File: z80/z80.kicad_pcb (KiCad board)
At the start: 2 copper layers, 19 parts, among them J1 Conn_02x16_Counter_Clockwise, J2 Conn_02x16_Counter_Clockwise, SW1 SW_DIP_x08, U1 74HC595, U12 74LS174, U13 74LS174, U18 74LS174, U2 74HC595, U21 SST39SF040, U22 74LS174, U23 74LS174, X8.000Mhz1 TFT680

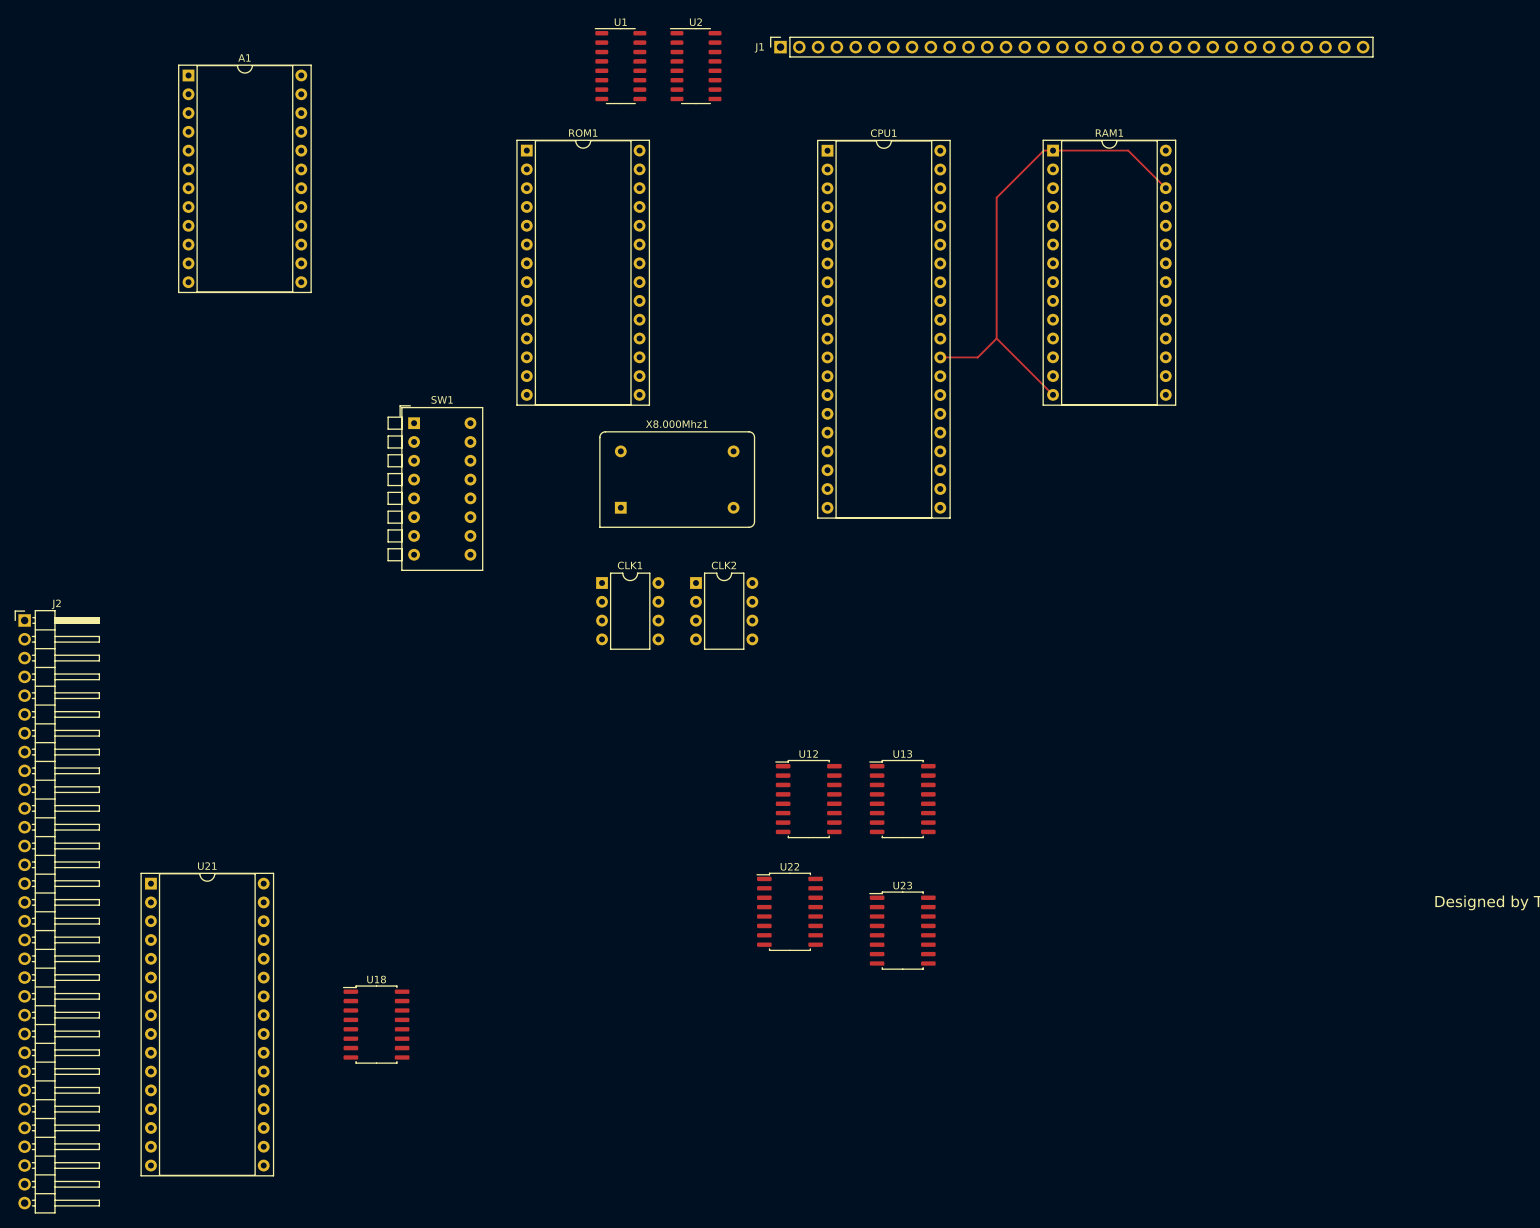
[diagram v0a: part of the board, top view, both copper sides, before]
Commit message: Schematic & eeprom programmer changes
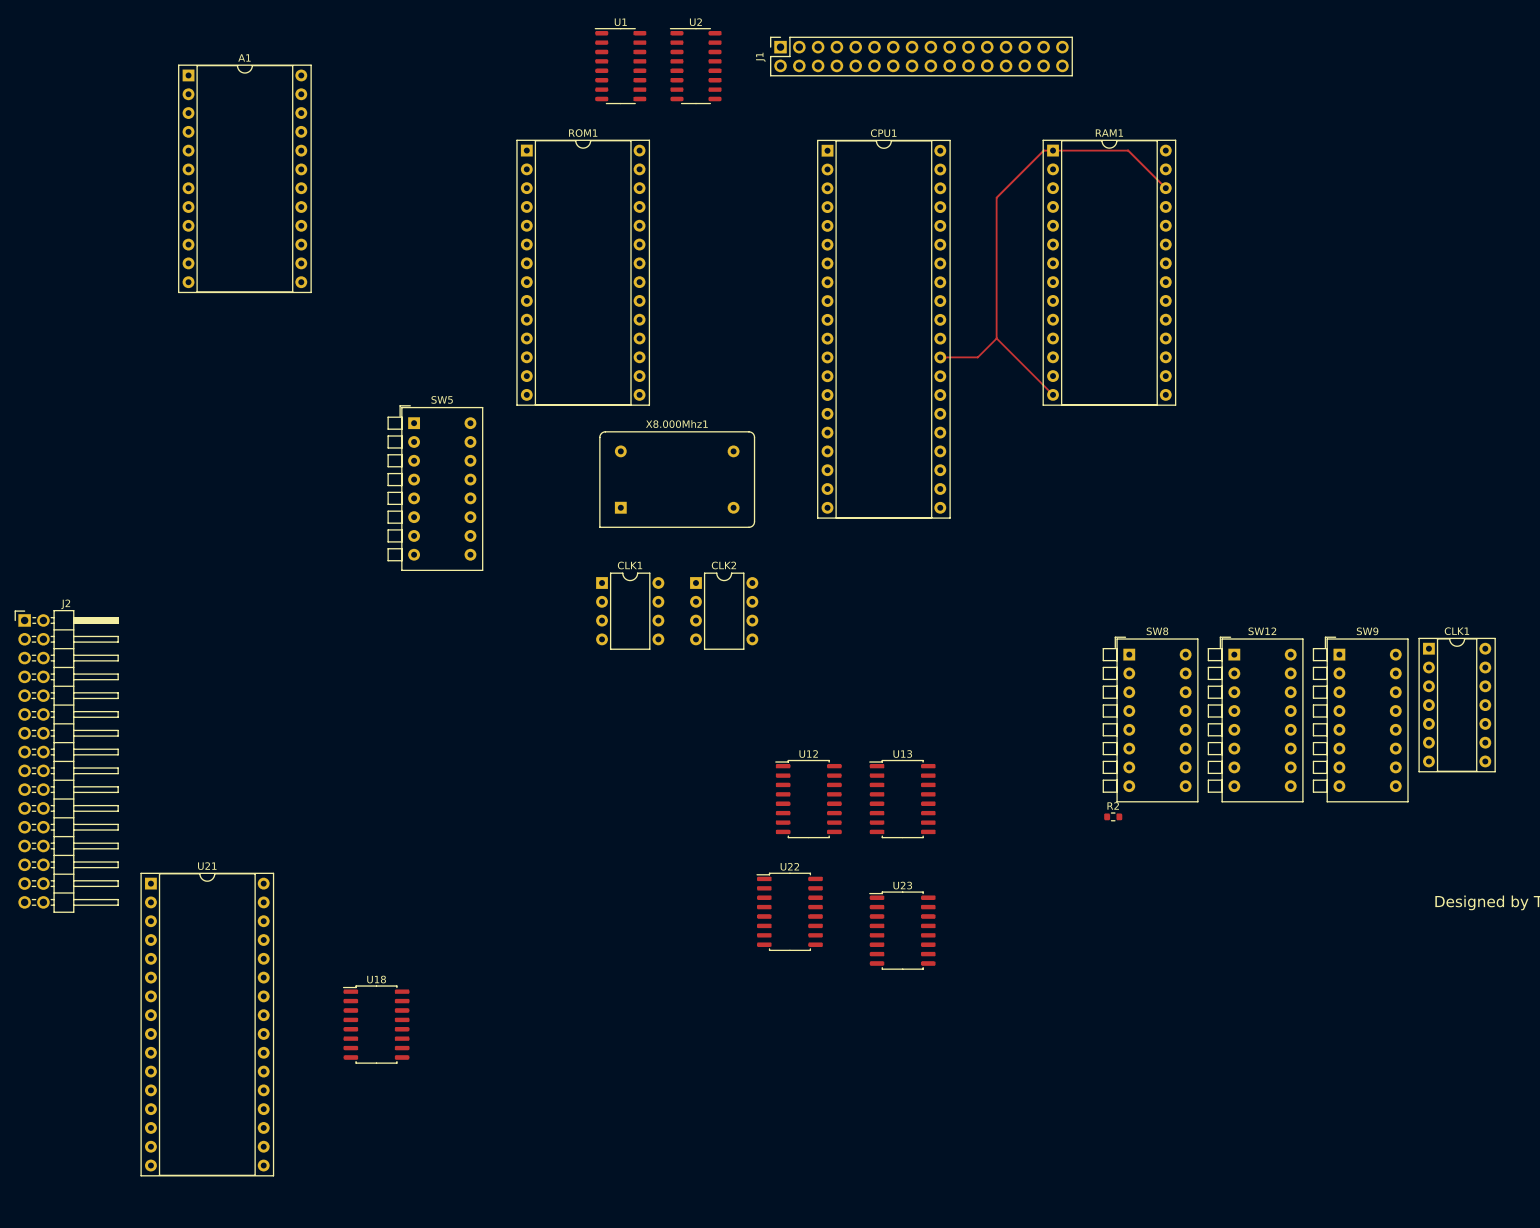
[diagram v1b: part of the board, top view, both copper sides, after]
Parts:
- added CLK1: NE556, Package_DIP:DIP-14_W7.62mm_Socket, F.Cu at (213.4, 119.4)
- added R2: 1K, Resistor_SMD:R_0603_1608Metric, F.Cu at (170.7, 142.1)
- added SW12: SW_DIP_x08, Button_Switch_THT:SW_DIP_SPSTx08_Piano_10.8x21.88mm_W7.62mm_P2.54mm, F.Cu at (187.1, 120.2)
- added SW8: SW_DIP_x08, Button_Switch_THT:SW_DIP_SPSTx08_Piano_10.8x21.88mm_W7.62mm_P2.54mm, F.Cu at (172.9, 120.2)
- added SW9: SW_DIP_x08, Button_Switch_THT:SW_DIP_SPSTx08_Piano_10.8x21.88mm_W7.62mm_P2.54mm, F.Cu at (201.3, 120.2)
- J1: footprint Connector_PinSocket_2.54mm:PinSocket_1x32_P2.54mm_Vertical -> Connector_PinSocket_2.54mm:PinSocket_2x16_P2.54mm_Vertical
- J2: footprint Connector_PinHeader_2.54mm:PinHeader_1x32_P2.54mm_Horizontal -> Connector_PinHeader_2.54mm:PinHeader_2x16_P2.54mm_Horizontal
- renumbered SW1 to SW5
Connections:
- net FstClk renamed /FstClk
- J1 pad 1: unconnected-(J1-Pad1) -> D7
- J1 pad 10: unconnected-(J1-Pad10) -> +5V
- J1 pad 16: unconnected-(J1-Pad16) -> GND
- J1 pad 17: unconnected-(J1-Pad17) -> GND
- J1 pad 18: unconnected-(J1-Pad18) -> A0
- J1 pad 19: unconnected-(J1-Pad19) -> A1
- J1 pad 2: unconnected-(J1-Pad2) -> D6
- J1 pad 20: unconnected-(J1-Pad20) -> A2
- J1 pad 21: unconnected-(J1-Pad21) -> A3
- J1 pad 22: unconnected-(J1-Pad22) -> A4
- J1 pad 23: unconnected-(J1-Pad23) -> A5
- J1 pad 24: unconnected-(J1-Pad24) -> A6
- J1 pad 25: unconnected-(J1-Pad25) -> A7
- J1 pad 26: unconnected-(J1-Pad26) -> A8
- J1 pad 27: unconnected-(J1-Pad27) -> A9
- J1 pad 28: unconnected-(J1-Pad28) -> A10
- J1 pad 29: unconnected-(J1-Pad29) -> A11
- J1 pad 3: unconnected-(J1-Pad3) -> D5
- J1 pad 30: unconnected-(J1-Pad30) -> A12
- J1 pad 31: unconnected-(J1-Pad31) -> A13
- J1 pad 32: unconnected-(J1-Pad32) -> A14
- J1 pad 4: unconnected-(J1-Pad4) -> D4
- J1 pad 5: unconnected-(J1-Pad5) -> D3
- J1 pad 6: unconnected-(J1-Pad6) -> D2
- J1 pad 7: unconnected-(J1-Pad7) -> D1
- J1 pad 8: unconnected-(J1-Pad8) -> D0
- J1 pad 9: unconnected-(J1-Pad9) -> A15
- X8.000Mhz1 pad 1: unconnected-(X8.000Mhz1-Pad1) -> GND

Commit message: schematic and pcb changes
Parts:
- removed the CLK1 at (101.6, 110.5)
- removed CLK2: NE555P, Package_DIP:DIP-8_W7.62mm
- added C1: 1uF, Capacitor_SMD:C_0805_2012Metric_Pad1.18x1.45mm_HandSolder, F.Cu at (133.3, 114.3)
- added C2: 0.1uF, Capacitor_SMD:C_0805_2012Metric_Pad1.18x1.45mm_HandSolder, F.Cu at (171.4, 120.7)
- added C3: 0.1uF, Capacitor_SMD:C_0805_2012Metric_Pad1.18x1.45mm_HandSolder, F.Cu at (144.8, 107.3)
- added C4: 0.1uF, Capacitor_SMD:C_0805_2012Metric_Pad1.18x1.45mm_HandSolder, F.Cu at (133.3, 119.4)
- added C5: 0.1uF, Capacitor_SMD:C_0805_2012Metric_Pad1.18x1.45mm_HandSolder, F.Cu at (133.3, 116.8)
- added C6: 0.1uF, Capacitor_SMD:C_0805_2012Metric_Pad1.18x1.45mm_HandSolder, F.Cu at (151.8, 125.7)
- added C7: 0.1uF, Capacitor_SMD:C_0805_2012Metric_Pad1.18x1.45mm_HandSolder, F.Cu at (151.1, 107.3)
- added D1: LED, LED_SMD:LED_0603_1608Metric_Pad1.05x0.95mm_HandSolder, F.Cu at (129.5, 121.9)
- added D10: LED_Small, LED_SMD:LED_0603_1608Metric_Pad1.05x0.95mm_HandSolder, F.Cu at (151.1, 58.4)
- added D11: LED_Small, LED_SMD:LED_0603_1608Metric_Pad1.05x0.95mm_HandSolder, F.Cu at (168.9, 46.4)
- added D12: LED_Small, LED_SMD:LED_0603_1608Metric_Pad1.05x0.95mm_HandSolder, F.Cu at (168.9, 43.8)
- added D13: LED_Small, LED_SMD:LED_0603_1608Metric_Pad1.05x0.95mm_HandSolder, F.Cu at (168.9, 41.3)
- added D14: LED_Small, LED_SMD:LED_0603_1608Metric_Pad1.05x0.95mm_HandSolder, F.Cu at (168.9, 38.7)
- added D15: LED_Small, LED_SMD:LED_0603_1608Metric_Pad1.05x0.95mm_HandSolder, F.Cu at (168.9, 36.2)
- added D16: LED_Small, LED_SMD:LED_0603_1608Metric_Pad1.05x0.95mm_HandSolder, F.Cu at (168.9, 33.7)
- added D17: LED_Small, LED_SMD:LED_0603_1608Metric_Pad1.05x0.95mm_HandSolder, F.Cu at (168.9, 31.1)
- added D18: LED_Small, LED_SMD:LED_0603_1608Metric_Pad1.05x0.95mm_HandSolder, F.Cu at (168.9, 28.6)
- added D19: LED_Small, LED_SMD:LED_0603_1608Metric_Pad1.05x0.95mm_HandSolder, F.Cu at (165.7, 88.9)
- added D2: LED, LED_SMD:LED_0603_1608Metric_Pad1.05x0.95mm_HandSolder, F.Cu at (129.5, 124.5)
- added D20: LED_Small, LED_SMD:LED_0603_1608Metric_Pad1.05x0.95mm_HandSolder, F.Cu at (165.7, 91.4)
- added D21: LED_Small, LED_SMD:LED_0603_1608Metric_Pad1.05x0.95mm_HandSolder, F.Cu at (165.7, 94.0)
- added D22: LED_Small, LED_SMD:LED_0603_1608Metric_Pad1.05x0.95mm_HandSolder, F.Cu at (165.7, 96.5)
- added D23: LED_Small, LED_SMD:LED_0603_1608Metric_Pad1.05x0.95mm_HandSolder, F.Cu at (165.7, 99.1)
- added D24: LED_Small, LED_SMD:LED_0603_1608Metric_Pad1.05x0.95mm_HandSolder, F.Cu at (165.7, 101.6)
- added D25: LED_Small, LED_SMD:LED_0603_1608Metric_Pad1.05x0.95mm_HandSolder, F.Cu at (165.7, 104.1)
- added D26: LED_Small, LED_SMD:LED_0603_1608Metric_Pad1.05x0.95mm_HandSolder, F.Cu at (165.7, 106.7)
- added D3: LED_Small, LED_SMD:LED_0603_1608Metric_Pad1.05x0.95mm_HandSolder, F.Cu at (151.1, 76.2)
- added D4: LED_Small, LED_SMD:LED_0603_1608Metric_Pad1.05x0.95mm_HandSolder, F.Cu at (151.1, 73.7)
- added D5: LED_Small, LED_SMD:LED_0603_1608Metric_Pad1.05x0.95mm_HandSolder, F.Cu at (151.1, 71.1)
- added D6: LED_Small, LED_SMD:LED_0603_1608Metric_Pad1.05x0.95mm_HandSolder, F.Cu at (151.1, 68.6)
- added D7: LED_Small, LED_SMD:LED_0603_1608Metric_Pad1.05x0.95mm_HandSolder, F.Cu at (151.1, 66.0)
- added D8: LED_Small, LED_SMD:LED_0603_1608Metric_Pad1.05x0.95mm_HandSolder, F.Cu at (151.1, 63.5)
- added D9: LED_Small, LED_SMD:LED_0603_1608Metric_Pad1.05x0.95mm_HandSolder, F.Cu at (151.1, 61.0)
- added R1: 1K, Resistor_SMD:R_0603_1608Metric_Pad0.98x0.95mm_HandSolder, F.Cu at (148.6, 125.7)
- added R10: 10K, Resistor_SMD:R_0603_1608Metric_Pad0.98x0.95mm_HandSolder, F.Cu at (133.3, 124.5)
- added R11: 1K, Resistor_SMD:R_0603_1608Metric_Pad0.98x0.95mm_HandSolder, F.Cu at (256.8, 114.0)
- added R12: 1K, Resistor_SMD:R_0603_1608Metric_Pad0.98x0.95mm_HandSolder, F.Cu at (154.9, 76.2)
- added R13: 1K, Resistor_SMD:R_0603_1608Metric_Pad0.98x0.95mm_HandSolder, F.Cu at (154.9, 73.7)
- added R14: 1K, Resistor_SMD:R_0603_1608Metric_Pad0.98x0.95mm_HandSolder, F.Cu at (154.9, 71.1)
- added R15: 1K, Resistor_SMD:R_0603_1608Metric_Pad0.98x0.95mm_HandSolder, F.Cu at (154.9, 68.6)
- added R16: 1K, Resistor_SMD:R_0603_1608Metric_Pad0.98x0.95mm_HandSolder, F.Cu at (154.9, 66.0)
- added R17: 1K, Resistor_SMD:R_0603_1608Metric_Pad0.98x0.95mm_HandSolder, F.Cu at (154.9, 63.5)
- added R18: 1K, Resistor_SMD:R_0603_1608Metric_Pad0.98x0.95mm_HandSolder, F.Cu at (154.9, 61.0)
- added R19: 1K, Resistor_SMD:R_0603_1608Metric_Pad0.98x0.95mm_HandSolder, F.Cu at (154.9, 58.4)
- added R2: 1K, Resistor_SMD:R_0603_1608Metric_Pad0.98x0.95mm_HandSolder, F.Cu at (154.9, 104.8)
- added R20: 1K, Resistor_SMD:R_0603_1608Metric_Pad0.98x0.95mm_HandSolder, F.Cu at (172.7, 46.4)
- added R21: 1K, Resistor_SMD:R_0603_1608Metric_Pad0.98x0.95mm_HandSolder, F.Cu at (172.7, 43.8)
- added R22: 1K, Resistor_SMD:R_0603_1608Metric_Pad0.98x0.95mm_HandSolder, F.Cu at (172.7, 41.3)
- added R23: 1K, Resistor_SMD:R_0603_1608Metric_Pad0.98x0.95mm_HandSolder, F.Cu at (172.7, 38.7)
- added R24: 1K, Resistor_SMD:R_0603_1608Metric_Pad0.98x0.95mm_HandSolder, F.Cu at (172.7, 36.2)
- added R25: 1K, Resistor_SMD:R_0603_1608Metric_Pad0.98x0.95mm_HandSolder, F.Cu at (172.7, 33.7)
- added R26: 1K, Resistor_SMD:R_0603_1608Metric_Pad0.98x0.95mm_HandSolder, F.Cu at (172.7, 31.1)
- added R27: 1K, Resistor_SMD:R_0603_1608Metric_Pad0.98x0.95mm_HandSolder, F.Cu at (172.7, 28.6)
- added R28: 1K, Resistor_SMD:R_0603_1608Metric_Pad0.98x0.95mm_HandSolder, F.Cu at (169.5, 88.9)
- added R29: 1K, Resistor_SMD:R_0603_1608Metric_Pad0.98x0.95mm_HandSolder, F.Cu at (169.5, 91.4)
- added R3: 10K, Resistor_SMD:R_0603_1608Metric_Pad0.98x0.95mm_HandSolder, F.Cu at (151.1, 95.9)
- added R30: 1K, Resistor_SMD:R_0603_1608Metric_Pad0.98x0.95mm_HandSolder, F.Cu at (169.5, 94.0)
- added R31: 1K, Resistor_SMD:R_0603_1608Metric_Pad0.98x0.95mm_HandSolder, F.Cu at (169.5, 96.5)
- added R32: 1K, Resistor_SMD:R_0603_1608Metric_Pad0.98x0.95mm_HandSolder, F.Cu at (169.5, 99.1)
- added R33: 1K, Resistor_SMD:R_0603_1608Metric_Pad0.98x0.95mm_HandSolder, F.Cu at (169.5, 101.6)
- added R34: 1K, Resistor_SMD:R_0603_1608Metric_Pad0.98x0.95mm_HandSolder, F.Cu at (169.5, 104.1)
- added R35: 1K, Resistor_SMD:R_0603_1608Metric_Pad0.98x0.95mm_HandSolder, F.Cu at (169.5, 106.7)
- added R36: 1K, Resistor_SMD:R_0603_1608Metric_Pad0.98x0.95mm_HandSolder, F.Cu at (198.8, 177.8)
- added R37: 10K, Resistor_SMD:R_0603_1608Metric_Pad0.98x0.95mm_HandSolder, F.Cu at (257.2, 111.5)
- added R38: 10K, Resistor_SMD:R_0603_1608Metric_Pad0.98x0.95mm_HandSolder, F.Cu at (225.3, 135.4)
- added R39: 1K, Resistor_SMD:R_0603_1608Metric_Pad0.98x0.95mm_HandSolder, F.Cu at (242.8, 131.8)
- added R4: 10K, Resistor_SMD:R_0603_1608Metric_Pad0.98x0.95mm_HandSolder, F.Cu at (151.1, 101.0)
- added R40: 1K, Resistor_SMD:R_0603_1608Metric_Pad0.98x0.95mm_HandSolder, F.Cu at (238.4, 131.8)
- added R41: 1K, Resistor_SMD:R_0603_1608Metric_Pad0.98x0.95mm_HandSolder, F.Cu at (221.0, 135.6)
- added R42: 10K, Resistor_SMD:R_0603_1608Metric_Pad0.98x0.95mm_HandSolder, F.Cu at (243.3, 116.7)
- added R43: 10K, Resistor_SMD:R_0603_1608Metric_Pad0.98x0.95mm_HandSolder, F.Cu at (229.7, 127.4)
- added R44: 10K, Resistor_SMD:R_0603_1608Metric_Pad0.98x0.95mm_HandSolder, F.Cu at (252.0, 116.5)
- added R45: 10K, Resistor_SMD:R_0603_1608Metric_Pad0.98x0.95mm_HandSolder, F.Cu at (234.1, 129.7)
- added R46: 10K, Resistor_SMD:R_0603_1608Metric_Pad0.98x0.95mm_HandSolder, F.Cu at (234.6, 119.7)
- added R47: 10K, Resistor_SMD:R_0603_1608Metric_Pad0.98x0.95mm_HandSolder, F.Cu at (238.9, 121.7)
- added R48: 10K, Resistor_SMD:R_0603_1608Metric_Pad0.98x0.95mm_HandSolder, F.Cu at (244.2, 111.5)
- added R49: 1K, Resistor_SMD:R_0603_1608Metric_Pad0.98x0.95mm_HandSolder, F.Cu at (247.6, 121.6)
- added R5: 10K, Resistor_SMD:R_0603_1608Metric_Pad0.98x0.95mm_HandSolder, F.Cu at (161.3, 98.4)
- added R50: 10K, Resistor_SMD:R_0603_1608Metric_Pad0.98x0.95mm_HandSolder, F.Cu at (243.3, 124.2)
- added R51: 1K, Resistor_SMD:R_0603_1608Metric_Pad0.98x0.95mm_HandSolder, F.Cu at (247.6, 124.1)
- added R7: 1K, Resistor_SMD:R_0603_1608Metric_Pad0.98x0.95mm_HandSolder, F.Cu at (134.0, 109.9)
- added R8: 2M, Resistor_SMD:R_0603_1608Metric_Pad0.98x0.95mm_HandSolder, F.Cu at (148.0, 105.4)
- added R9: 10K, Resistor_SMD:R_0603_1608Metric_Pad0.98x0.95mm_HandSolder, F.Cu at (133.3, 121.9)
- added SW13: SW_DIP_x08, Button_Switch_THT:SW_DIP_SPSTx08_Piano_10.8x21.88mm_W7.62mm_P2.54mm, F.Cu at (17.8, 49.5)
- added SW14: SW_DIP_x08, Button_Switch_THT:SW_DIP_SPSTx08_Piano_10.8x21.88mm_W7.62mm_P2.54mm, F.Cu at (32.0, 49.5)
- added U1: 4081, Package_SO:SO-14_3.9x8.65mm_P1.27mm, F.Cu at (156.2, 97.2)
- SW5: footprint Button_Switch_THT:SW_DIP_SPSTx08_Piano_10.8x21.88mm_W7.62mm_P2.54mm -> Button_Switch_THT:SW_DIP_SPSTx08_Slide_9.78x22.5mm_W7.62mm_P2.54mm
- moved SW10 151.4 mm to (55.5, 79.4)
- moved SW12 151.4 mm to (41.3, 79.4)
- moved SW9 151.2 mm to (27.3, 79.4)
- moved CLK1 75.9 mm to (137.8, 111.8)
- moved U2 64.3 mm to (40.6, 30.5)
- moved U3 64.3 mm to (50.8, 30.5)
- moved X8.000Mhz1 63.5 mm to (166.4, 113.0), turned to 180 degrees
- moved R6 46.1 mm to (139.1, 108.6), turned to 180 degrees
- moved SW5 29.7 mm to (104.2, 98.8), turned to 90 degrees
- moved ROM1 10.2 mm to (101.6, 52.1)
- moved J1 2.52 mm to (125.7, 35.6)
- renumbered R2 to R6, SW9 to SW10, SW8 to SW9, U12 to U14, U13 to U15, U1 to U2, U18 to U20, U21 to U23, U22 to U24, U23 to U25, U2 to U3
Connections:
- CLK1 pad 5: +5V -> /AdjClk
- CPU1 pad 16: unconnected-(CPU1-Pad16) -> /INT
- CPU1 pad 17: unconnected-(CPU1-Pad17) -> /NMI
- CPU1 pad 19: MemReq -> /MREQ
- CPU1 pad 20: IOReq -> /IORQ
- J1 pad 11: unconnected-(J1-Pad11) -> /RST
- J1 pad 12: unconnected-(J1-Pad12) -> /IORQ
- J1 pad 13: unconnected-(J1-Pad13) -> /MREQ
- J1 pad 14: unconnected-(J1-Pad14) -> RD
- J1 pad 15: unconnected-(J1-Pad15) -> WR
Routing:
- net +5V: track 0.00 -> 209.1 mm, vias 0 -> 3
- net A11: track 0.00 -> 95.9 mm, vias 0 -> 2
- net A12: track 0.00 -> 90.0 mm, vias 0 -> 1
- net D6: track 0.00 -> 88.5 mm, vias 0 -> 3
- net /MREQ: track 0.00 -> 88.4 mm
- net A8: track 0.00 -> 86.2 mm, vias 0 -> 3
- net A9: track 0.00 -> 83.8 mm, vias 0 -> 2
- net D4: track 0.00 -> 82.7 mm, vias 0 -> 2
- net D5: track 0.00 -> 81.8 mm, vias 0 -> 4
- net A10: track 0.00 -> 77.4 mm, vias 0 -> 1
- net /IORQ: track 0.00 -> 75.5 mm, vias 0 -> 1
- net D3: track 0.00 -> 74.4 mm
- net D7: track 0.00 -> 74.2 mm, vias 0 -> 2
- net A15: track 0.00 -> 72.0 mm
- net A1: track 0.00 -> 69.5 mm
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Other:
- board outline added: 224.2 x 181 mm
- board text added: "A0"
- board text added: "A1"
- board text added: "A10"
- board text added: "A11"
- board text added: "A12"
- board text added: "A13"
- board text added: "A14"
- board text added: "A15"
- board text added: "A2"
- board text added: "A3"
- board text added: "A4"
- board text added: "A5"
- board text added: "A6"
- board text added: "A7"
- board text added: "A8"
- board text added: "A9"
- board text added: "D0"
- board text added: "D1"
- board text added: "D2"
- board text added: "D3"
- board text added: "D4"
- board text added: "D5"
- board text added: "D6"
- board text added: "D7"

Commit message: cleaned up files, added script to launch programming tool
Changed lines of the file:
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@@
     (pad_to_mask_clearance 0)
     (pcbplotparams
-      (layerselection 0x00010fc_ffffffff)
+      (layerselection 0x00000fc_ffffffff)
       (disableapertmacros false)
       (usegerberextensions false)
@@
     (fp_line (start 1 -0.625) (end 1 0.625) (layer "F.Fab") (width 0.1))
     (fp_line (start -1 -0.625) (end 1 -0.625) (layer "F.Fab") (width 0.1))
-    (pad "1" smd roundrect (at -1.0375 0 180) (size 1.175 1.45) (layers "F.Cu" "F.Paste" "F.Mask") (roundrect_rratio 0.212766)
+    (pad "1" smd roundrect (at -1.0375 0 180) (size 1.175 1.45) (layers "F.Cu" "F.Paste" "F.Mask") (roundrect_rratio 0.2127659574)
       (net 28 "GND") (pintype "passive"))
-    (pad "2" smd roundrect (at 1.0375 0 180) (size 1.175 1.45) (layers "F.Cu" "F.Paste" "F.Mask") (roundrect_rratio 0.212766)
+    (pad "2" smd roundrect (at 1.0375 0 180) (size 1.175 1.45) (layers "F.Cu" "F.Paste" "F.Mask") (roundrect_rratio 0.2127659574)
       (net 33 "Net-(C7-Pad2)") (pintype "passive"))
     (model "${KICAD6_3DMODEL_DIR}/Capacitor_SMD.3dshapes/C_0805_2012Metric.wrl"
@@
     (fp_line (start -1 0.625) (end -1 -0.625) (layer "F.Fab") (width 0.1))
     (fp_line (start 1 -0.625) (end 1 0.625) (layer "F.Fab") (width 0.1))
-    (pad "1" smd roundrect (at -1.0375 0 180) (size 1.175 1.45) (layers "F.Cu" "F.Paste" "F.Mask") (roundrect_rratio 0.212766)
+    (pad "1" smd roundrect (at -1.0375 0 180) (size 1.175 1.45) (layers "F.Cu" "F.Paste" "F.Mask") (roundrect_rratio 0.2127659574)
       (net 31 "Net-(C5-Pad1)") (pintype "passive"))
-    (pad "2" smd roundrect (at 1.0375 0 180) (size 1.175 1.45) (layers "F.Cu" "F.Paste" "F.Mask") (roundrect_rratio 0.212766)
+    (pad "2" smd roundrect (at 1.0375 0 180) (size 1.175 1.45) (layers "F.Cu" "F.Paste" "F.Mask") (roundrect_rratio 0.2127659574)
       (net 28 "GND") (pintype "passive"))
     (model "${KICAD6_3DMODEL_DIR}/Capacitor_SMD.3dshapes/C_0805_2012Metric.wrl"
@@
     (fp_line (start 1 0.625) (end -1 0.625) (layer "F.Fab") (width 0.1))
     (fp_line (start -1 0.625) (end -1 -0.625) (layer "F.Fab") (width 0.1))
-    (pad "1" smd roundrect (at -1.0375 0) (size 1.175 1.45) (layers "F.Cu" "F.Paste" "F.Mask") (roundrect_rratio 0.212766)
+    (pad "1" smd roundrect (at -1.0375 0) (size 1.175 1.45) (layers "F.Cu" "F.Paste" "F.Mask") (roundrect_rratio 0.2127659574)
       (net 28 "GND") (pintype "passive"))
-    (pad "2" smd roundrect (at 1.0375 0) (size 1.175 1.45) (layers "F.Cu" "F.Paste" "F.Mask") (roundrect_rratio 0.212766)
+    (pad "2" smd roundrect (at 1.0375 0) (size 1.175 1.45) (layers "F.Cu" "F.Paste" "F.Mask") (roundrect_rratio 0.2127659574)
       (net 30 "+5V") (pintype "passive"))
     (model "${KICAD6_3DMODEL_DIR}/Capacitor_SMD.3dshapes/C_0805_2012Metric.wrl"
@@
     (fp_line (start -1 -0.625) (end 1 -0.625) (layer "F.Fab") (width 0.1))
     (fp_line (start 1 0.625) (end -1 0.625) (layer "F.Fab") (width 0.1))
-    (pad "1" smd roundrect (at -1.0375 0 180) (size 1.175 1.45) (layers "F.Cu" "F.Paste" "F.Mask") (roundrect_rratio 0.212766)
+    (pad "1" smd roundrect (at -1.0375 0 180) (size 1.175 1.45) (layers "F.Cu" "F.Paste" "F.Mask") (roundrect_rratio 0.2127659574)
       (net 28 "GND") (pintype "passive"))
-    (pad "2" smd roundrect (at 1.0375 0 180) (size 1.175 1.45) (layers "F.Cu" "F.Paste" "F.Mask") (roundrect_rratio 0.212766)
+    (pad "2" smd roundrect (at 1.0375 0 180) (size 1.175 1.45) (layers "F.Cu" "F.Paste" "F.Mask") (roundrect_rratio 0.2127659574)
       (net 30 "+5V") (pintype "passive"))
     (model "${KICAD6_3DMODEL_DIR}/Capacitor_SMD.3dshapes/C_0805_2012Metric.wrl"
@@
     (fp_line (start -1 0.625) (end -1 -0.625) (layer "F.Fab") (width 0.1))
     (fp_line (start -1 -0.625) (end 1 -0.625) (layer "F.Fab") (width 0.1))
-    (pad "1" smd roundrect (at -1.0375 0 180) (size 1.175 1.45) (layers "F.Cu" "F.Paste" "F.Mask") (roundrect_rratio 0.212766)
+    (pad "1" smd roundrect (at -1.0375 0 180) (size 1.175 1.45) (layers "F.Cu" "F.Paste" "F.Mask") (roundrect_rratio 0.2127659574)
       (net 28 "GND") (pintype "passive"))
-    (pad "2" smd roundrect (at 1.0375 0 180) (size 1.175 1.45) (layers "F.Cu" "F.Paste" "F.Mask") (roundrect_rratio 0.212766)
+    (pad "2" smd roundrect (at 1.0375 0 180) (size 1.175 1.45) (layers "F.Cu" "F.Paste" "F.Mask") (roundrect_rratio 0.2127659574)
       (net 30 "+5V") (pintype "passive"))
     (model "${KICAD6_3DMODEL_DIR}/Capacitor_SMD.3dshapes/C_0805_2012Metric.wrl"
@@
     (fp_line (start -1 0.625) (end -1 -0.625) (layer "F.Fab") (width 0.1))
     (fp_line (start 1 0.625) (end -1 0.625) (layer "F.Fab") (width 0.1))
-    (pad "1" smd roundrect (at -1.0375 0 180) (size 1.175 1.45) (layers "F.Cu" "F.Paste" "F.Mask") (roundrect_rratio 0.212766)
+    (pad "1" smd roundrect (at -1.0375 0 180) (size 1.175 1.45) (layers "F.Cu" "F.Paste" "F.Mask") (roundrect_rratio 0.2127659574)
       (net 29 "Net-(C1-Pad1)") (pintype "passive"))
-    (pad "2" smd roundrect (at 1.0375 0 180) (size 1.175 1.45) (layers "F.Cu" "F.Paste" "F.Mask") (roundrect_rratio 0.212766)
+    (pad "2" smd roundrect (at 1.0375 0 180) (size 1.175 1.45) (layers "F.Cu" "F.Paste" "F.Mask") (roundrect_rratio 0.2127659574)
       (net 28 "GND") (pintype "passive"))
     (model "${KICAD6_3DMODEL_DIR}/Capacitor_SMD.3dshapes/C_0805_2012Metric.wrl"
@@
     (fp_line (start -1 -0.625) (end 1 -0.625) (layer "F.Fab") (width 0.1))
     (fp_line (start -1 0.625) (end -1 -0.625) (layer "F.Fab") (width 0.1))
-    (pad "1" smd roundrect (at -1.0375 0 270) (size 1.175 1.45) (layers "F.Cu" "F.Paste" "F.Mask") (roundrect_rratio 0.212766)
+    (pad "1" smd roundrect (at -1.0375 0 270) (size 1.175 1.45) (layers "F.Cu" "F.Paste" "F.Mask") (roundrect_rratio 0.2127659574)
       (net 32 "Net-(C6-Pad1)") (pintype "passive"))
-    (pad "2" smd roundrect (at 1.0375 0 270) (size 1.175 1.45) (layers "F.Cu" "F.Paste" "F.Mask") (roundrect_rratio 0.212766)
+    (pad "2" smd roundrect (at 1.0375 0 270) (size 1.175 1.45) (layers "F.Cu" "F.Paste" "F.Mask") (roundrect_rratio 0.2127659574)
       (net 28 "GND") (pintype "passive"))
     (model "${KICAD6_3DMODEL_DIR}/Capacitor_SMD.3dshapes/C_0805_2012Metric.wrl"
